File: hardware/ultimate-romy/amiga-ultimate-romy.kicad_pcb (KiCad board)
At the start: 2 copper layers, 39.4 x 39.4 mm, 7 parts, among them IC2 FAT_GARY, U1 ATF22V10C-XU, U2 ATF22V10C-XU

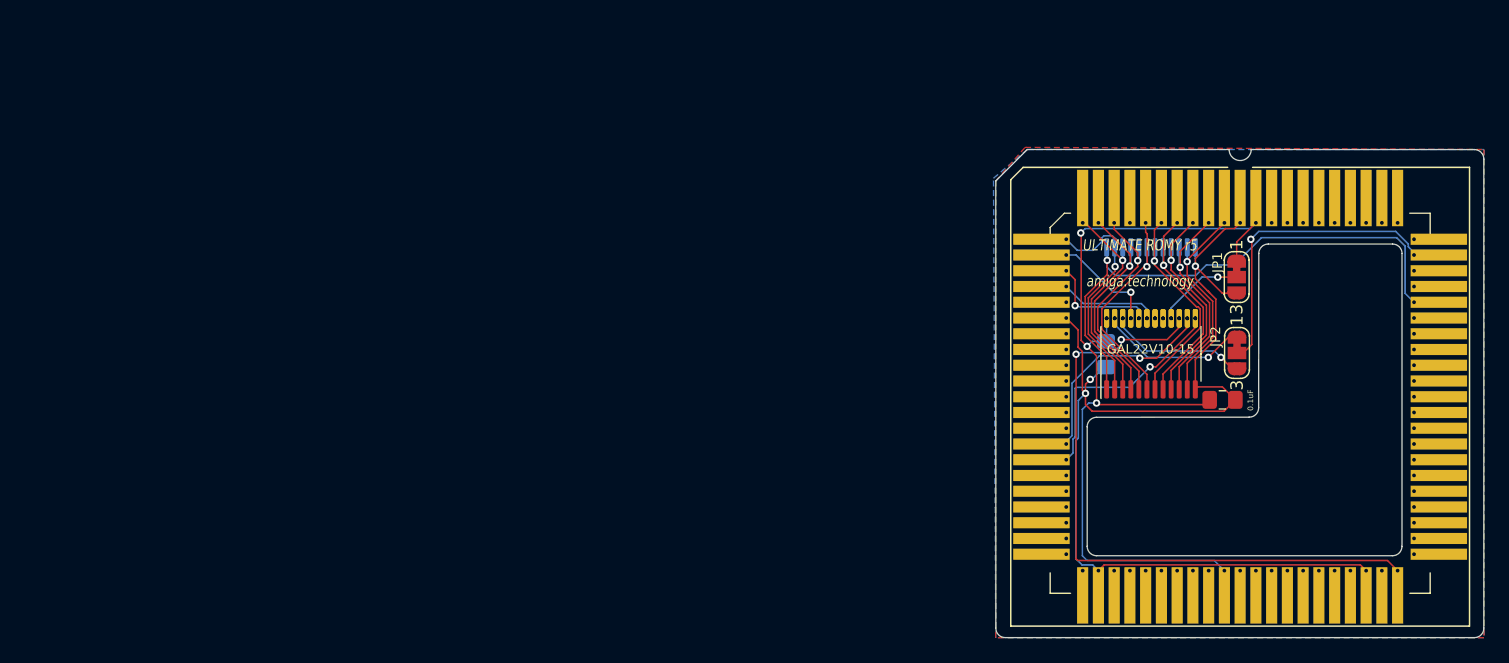
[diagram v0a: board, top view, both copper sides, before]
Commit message: Update Ultimate ROMY to Rev6
- Reroute the board to use 6mil instead of 5mil traces.
  This will make the boards significantly cheaper with some fab houses
- Add address pins for 4MB support
- Move vias in PLCC footprint to the outside to prevent solder paste
  from leaking to the other side when using hot air to assemble socket
  on A4000 version
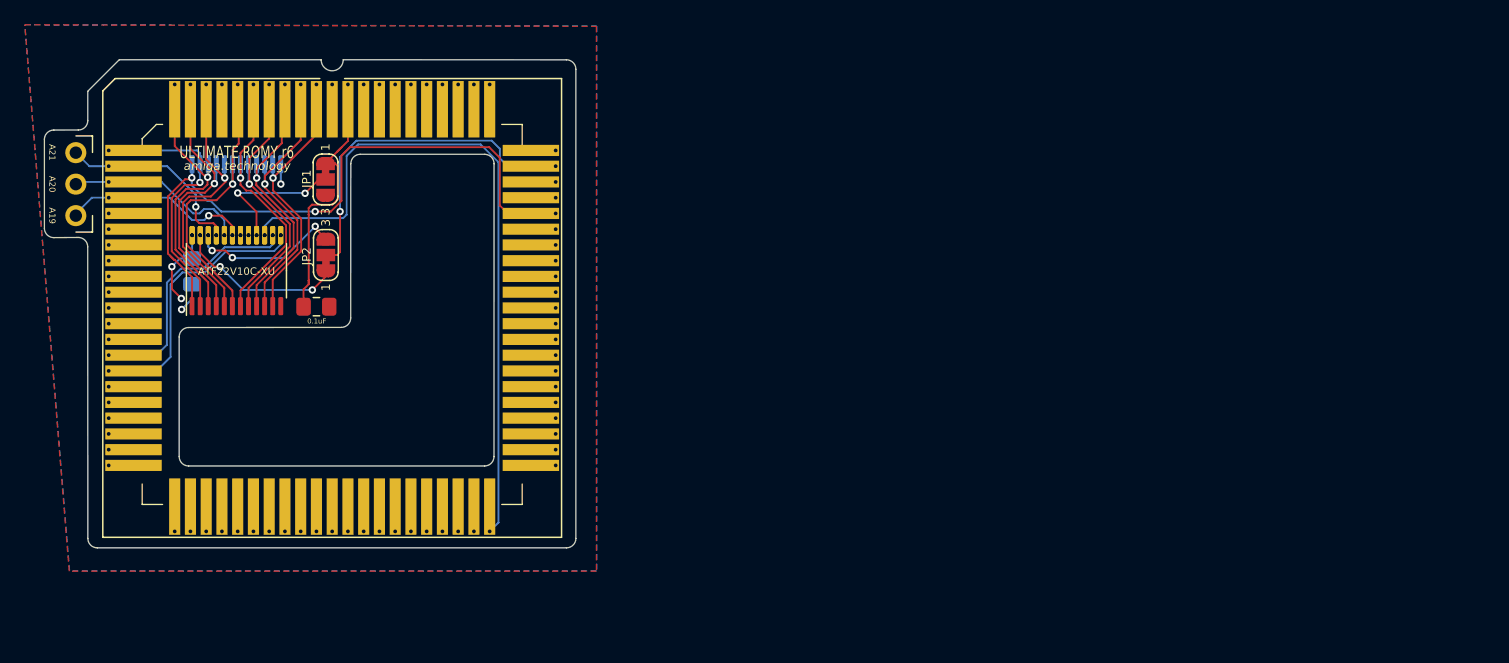
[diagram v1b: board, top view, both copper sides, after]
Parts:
- added J1: Conn_01x03_Male, amiga-romy:Address_PinHeader_1x03_P2.54mm_Vertical, F.Cu at (21.1, 43.4)
- added カツ: Katsu, amiga-romy:Katsu, F.Cu at (35.7, 54.1)
- IC2: footprint amiga-romy:APW9328TH -> amiga-romy:APW9328THO
- moved U1 74.1 mm to (34.0, 53.0)
- moved U2 74.1 mm to (34.0, 47.2)
- moved C2 74.0 mm to (30.4, 53.0)
- moved JP2 73.9 mm to (41.2, 51.7), turned to 90 degrees
- moved JP1 73.9 mm to (41.2, 45.6)
- moved IC2 73.6 mm to (41.7, 56.0)
- moved C1 73.5 mm to (40.5, 55.9)
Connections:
- net /GND renamed GND
- net /VCC renamed VCC
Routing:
- net GND: track 87.6 -> 3.98 mm, vias 3 -> 2
- net VCC: track 70.9 -> 29.0 mm, vias 3 -> 2
- net /I1/CLK: track 44.2 -> 53.5 mm, vias 1 -> 2
- net /IO5: track 8.00 -> 15.3 mm, vias 0 -> 1
- net /IO3: track 9.07 -> 15.7 mm
- net /IO4: track 9.11 -> 15.3 mm, vias 1 -> 0
- net /I6: track 18.2 -> 24.1 mm
- net /I5: track 18.0 -> 23.6 mm
- net /I9: track 17.6 -> 22.9 mm
- net /I4: track 18.5 -> 23.5 mm
- net /I3: track 18.0 -> 23.1 mm
- net /I8: track 18.0 -> 22.9 mm
- net /I10: track 18.0 -> 22.8 mm
- net /I11: track 17.5 -> 22.3 mm
- net /I7: track 18.0 -> 22.7 mm
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- added copper zone on B.Cu, net VCC
- removed copper zone on B.Cu, net GND
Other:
- board size 39.4 x 39.4 mm -> 42.9 x 39.4 mm
- board text added: "CREDITS GO TO SPEEDGEEK, COSMOS, ACILL, FLOREN, CDH, NOTTHEMATZE"
- board text added: "ULTIMATE ROMY r6"
- board text added: "amiga.technology"
- board text removed: "0.1uF"
- board text removed: "GAL22V10-15"
- board text removed: "ULTIMATE ROMY r5 amiga.technology"
- board text removed: "カツ"
